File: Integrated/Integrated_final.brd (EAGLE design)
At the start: 201.9 x 77.1 mm, 73 parts, among them IC1 74AHC1G32DBV, IC2 74AHC1G08DBV, IC3 74AHC1G08DBV, IC7 74AHC1G32DBV, Q1 PSMN013-30MLC, Q2 PSMN013-30MLC, Q3 PSMN013-30MLC, Q4 PSMN013-30MLC, Q5 PSMN013-30MLC, Q6 PSMN013-30MLC, X1 5566-4, X2 5566-4

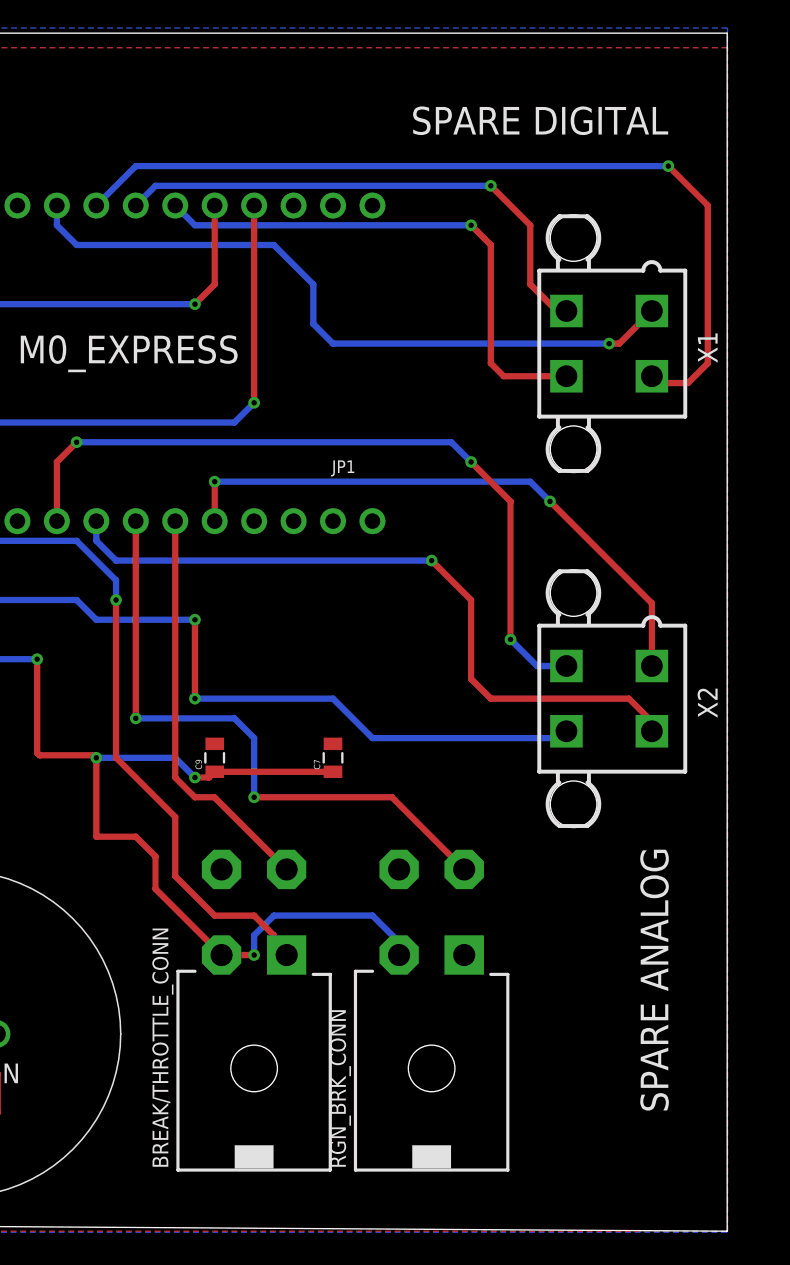
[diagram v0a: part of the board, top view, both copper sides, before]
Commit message: changed connectors to spare digital and analog to 90 degree 4 pin molex minifit
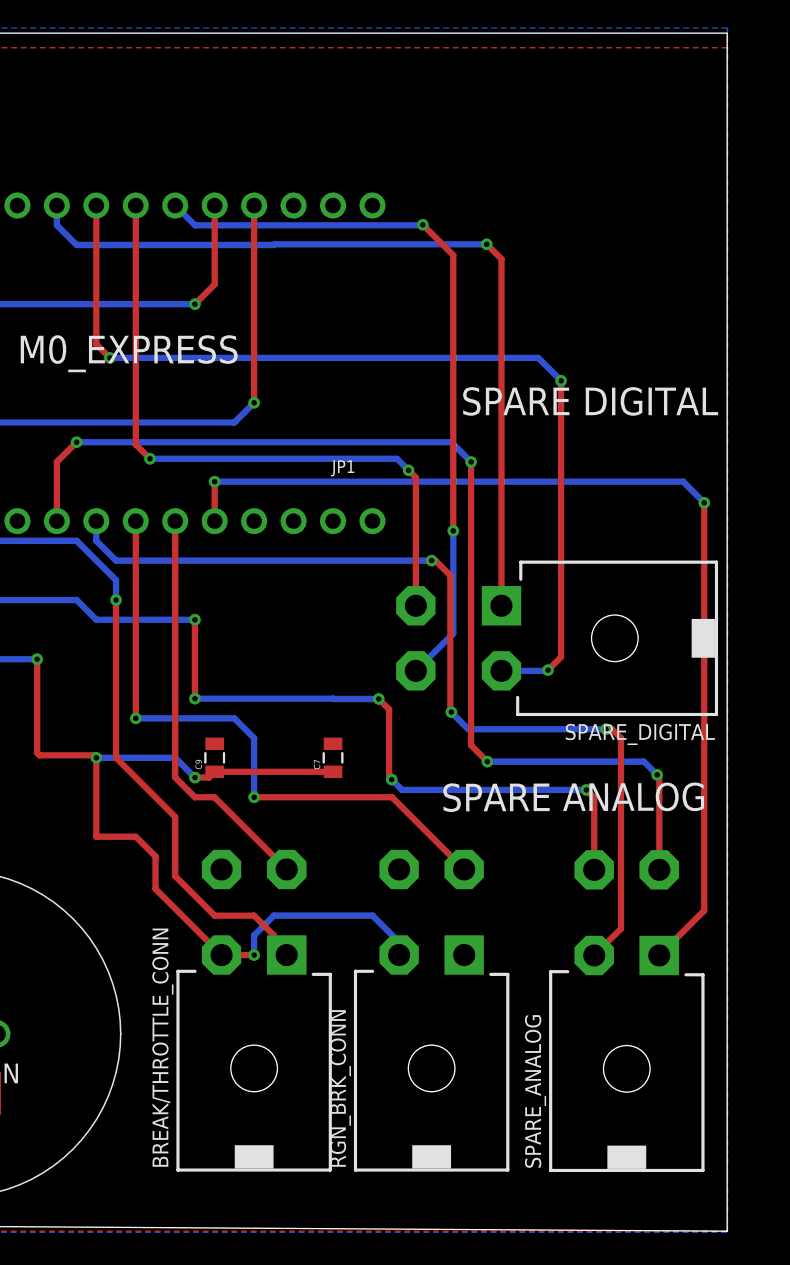
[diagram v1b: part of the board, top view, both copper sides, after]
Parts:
- removed X1, X2: 5566-4, con-molex:5566-4
- added SPARE_ANALOG, SPARE_DIGITAL: 39-30-04?, con-molex-mini-fit:39-30-?04?
- C1, C2, C5, C6: value (none) -> 18 pF
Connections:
- net A0: now also SPARE_ANALOG.1; no longer X2.1
- net A3: now also SPARE_ANALOG.2; no longer X2.2
- net A4: now also SPARE_ANALOG.3; no longer X2.3
- net D0: now also SPARE_ANALOG.4; no longer X2.4
- net D10: now also SPARE_DIGITAL.4; no longer X1.4
- net D11: now also SPARE_DIGITAL.3; no longer X1.3
- net D12: now also SPARE_DIGITAL.2; no longer X1.2
- net D13: now also SPARE_DIGITAL.1; no longer X1.1
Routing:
- net A0: track 38.0 -> 65.0 mm
- net A4: track 48.3 -> 68.7 mm, vias 3 -> 4
- net A3: track 45.5 -> 60.1 mm, vias 1 -> 3
- net D10: track 34.2 -> 47.0 mm, vias 1 -> 2
- net D0: track 60.0 -> 70.4 mm, vias 3 -> 6
- net D11: track 33.8 -> 42.6 mm, vias 1 -> 2
- net D13: track 45.1 -> 53.2 mm
- net D12: track 55.9 -> 61.8 mm, vias 1 -> 3
